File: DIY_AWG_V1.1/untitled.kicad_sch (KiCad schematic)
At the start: 61 parts, among them U1 AMS1117-3.3, U2 ADP7118ARDZ-3.3-R7, U3 ADP7118ARDZ-3.3-R7, U4 TPS7A3301RGWR, U5 TPS7A4701RGWR, U6 TPS7A3301RGWR, U7 TPS7A4701RGWR

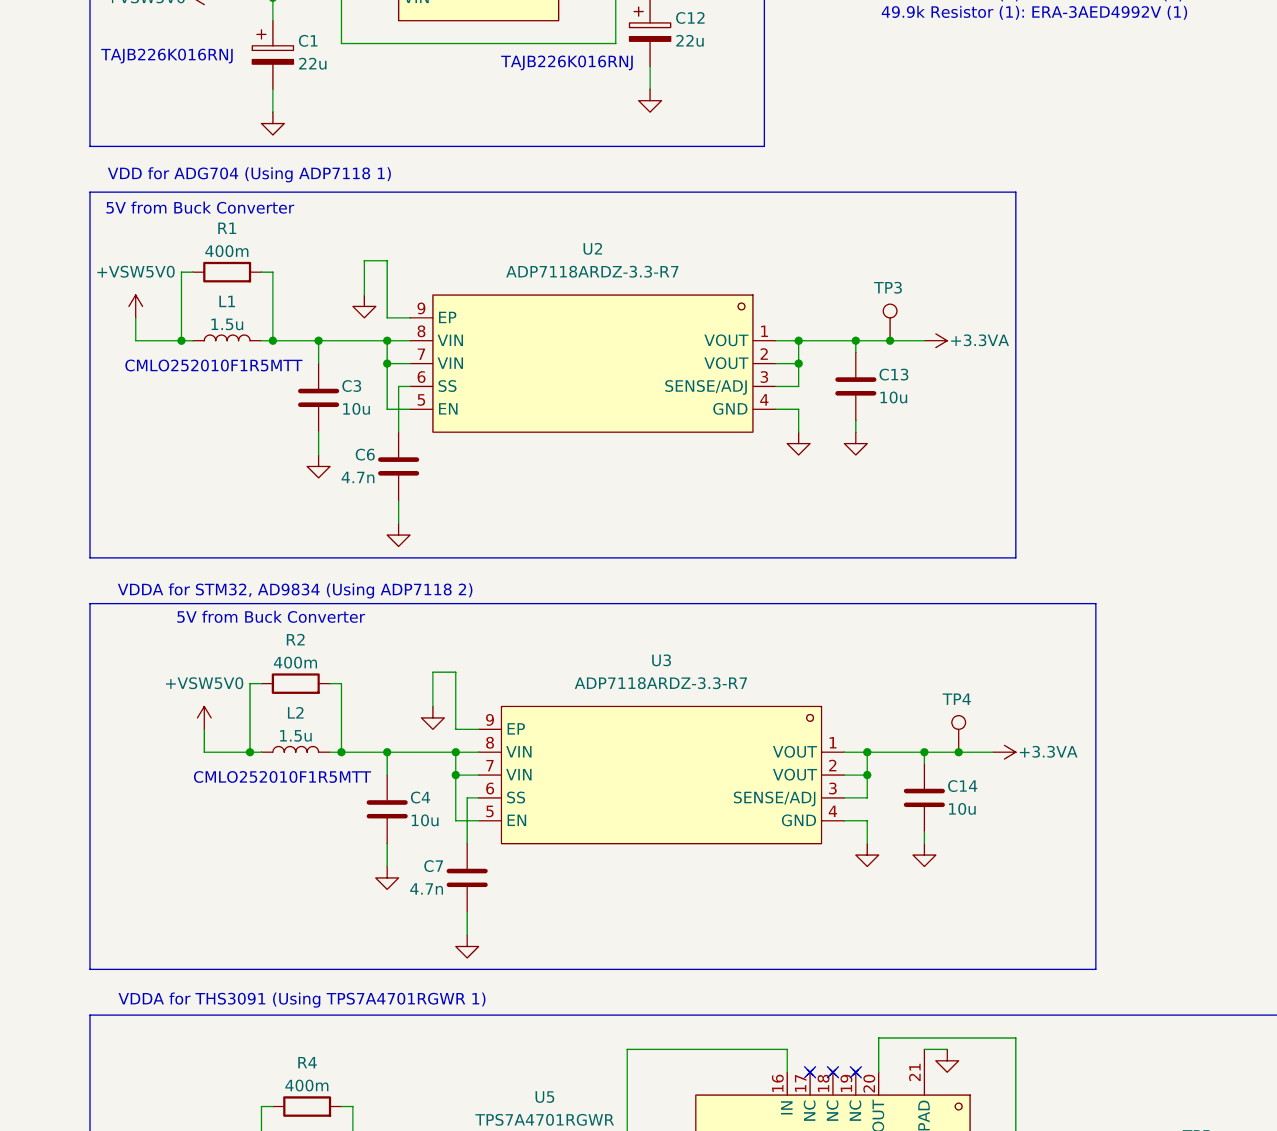
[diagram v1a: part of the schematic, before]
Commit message: Updated pin description of relevant components
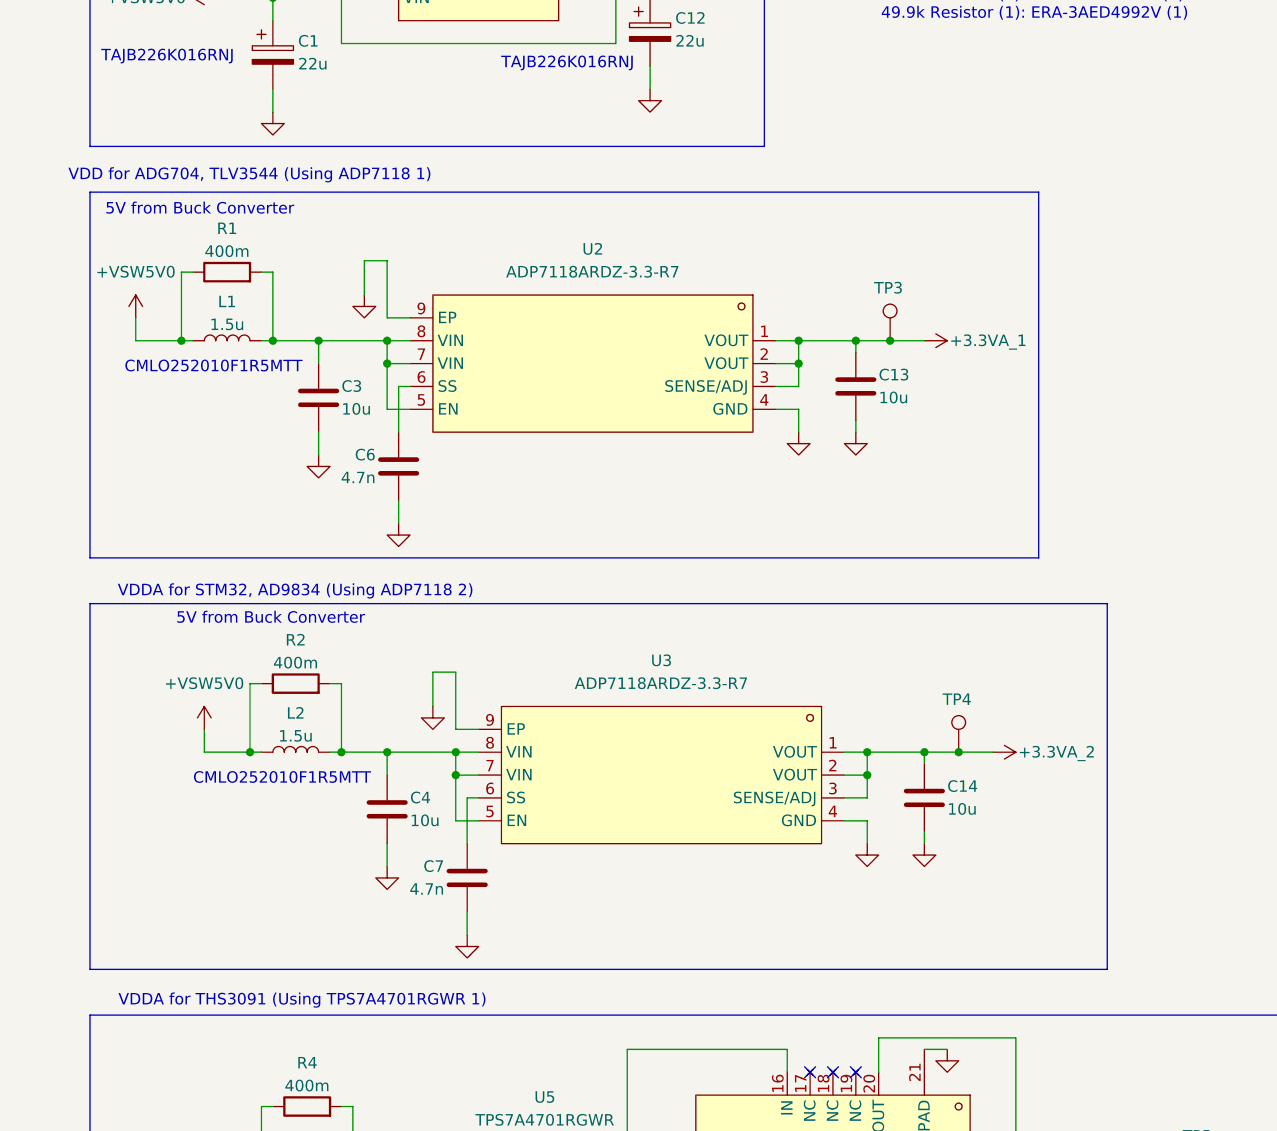
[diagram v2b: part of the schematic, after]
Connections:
- net +3.3VA renamed +3.3VA_1
- net +3.3VA_1: no longer C14.1, TP4.1, U3.1 (VOUT), U3.2 (VOUT), U3.3 (SENSE/ADJ)
- new net +3.3VA_2: C14.1, TP4.1, U3.1 (VOUT), U3.2 (VOUT), U3.3 (SENSE/ADJ)
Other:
- note added: "VDD for ADG704, TLV3544 (Using ADP7118 1)"
- note removed: "VDD for ADG704 (Using ADP7118 1)"
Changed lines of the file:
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@@
 	(rectangle
 		(start 15.24 118.11)
-		(end 127 158.75)
+		(end 128.27 158.75)
 		(stroke
 			(width 0)
@@
 	(rectangle
 		(start 15.24 72.39)
-		(end 118.11 113.03)
+		(end 120.65 113.03)
 		(stroke
 			(width 0)
@@
 		)
 	)
-	(text "VDD for ADG704 (Using ADP7118 1)\n\n"
+	(text "VDD for ADG704, TLV3544 (Using ADP7118 1)\n\n"
 		(exclude_from_sim no)
 		(at 33.02 71.628 0)
@@
 			)
 		)
-		(property "Value" "+3.3VA"
+		(property "Value" "+3.3VA_1"
 			(at 110.744 88.9 90)
 			(show_name no)
@@
 			)
 		)
-		(property "Value" "+3.3VA"
+		(property "Value" "+3.3VA_2"
 			(at 118.364 134.62 90)
 			(show_name no)

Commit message: Updated schematics to clear ERCs
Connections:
- net at C20.1, C22.1, L5.2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: now also U6.13 (EN)

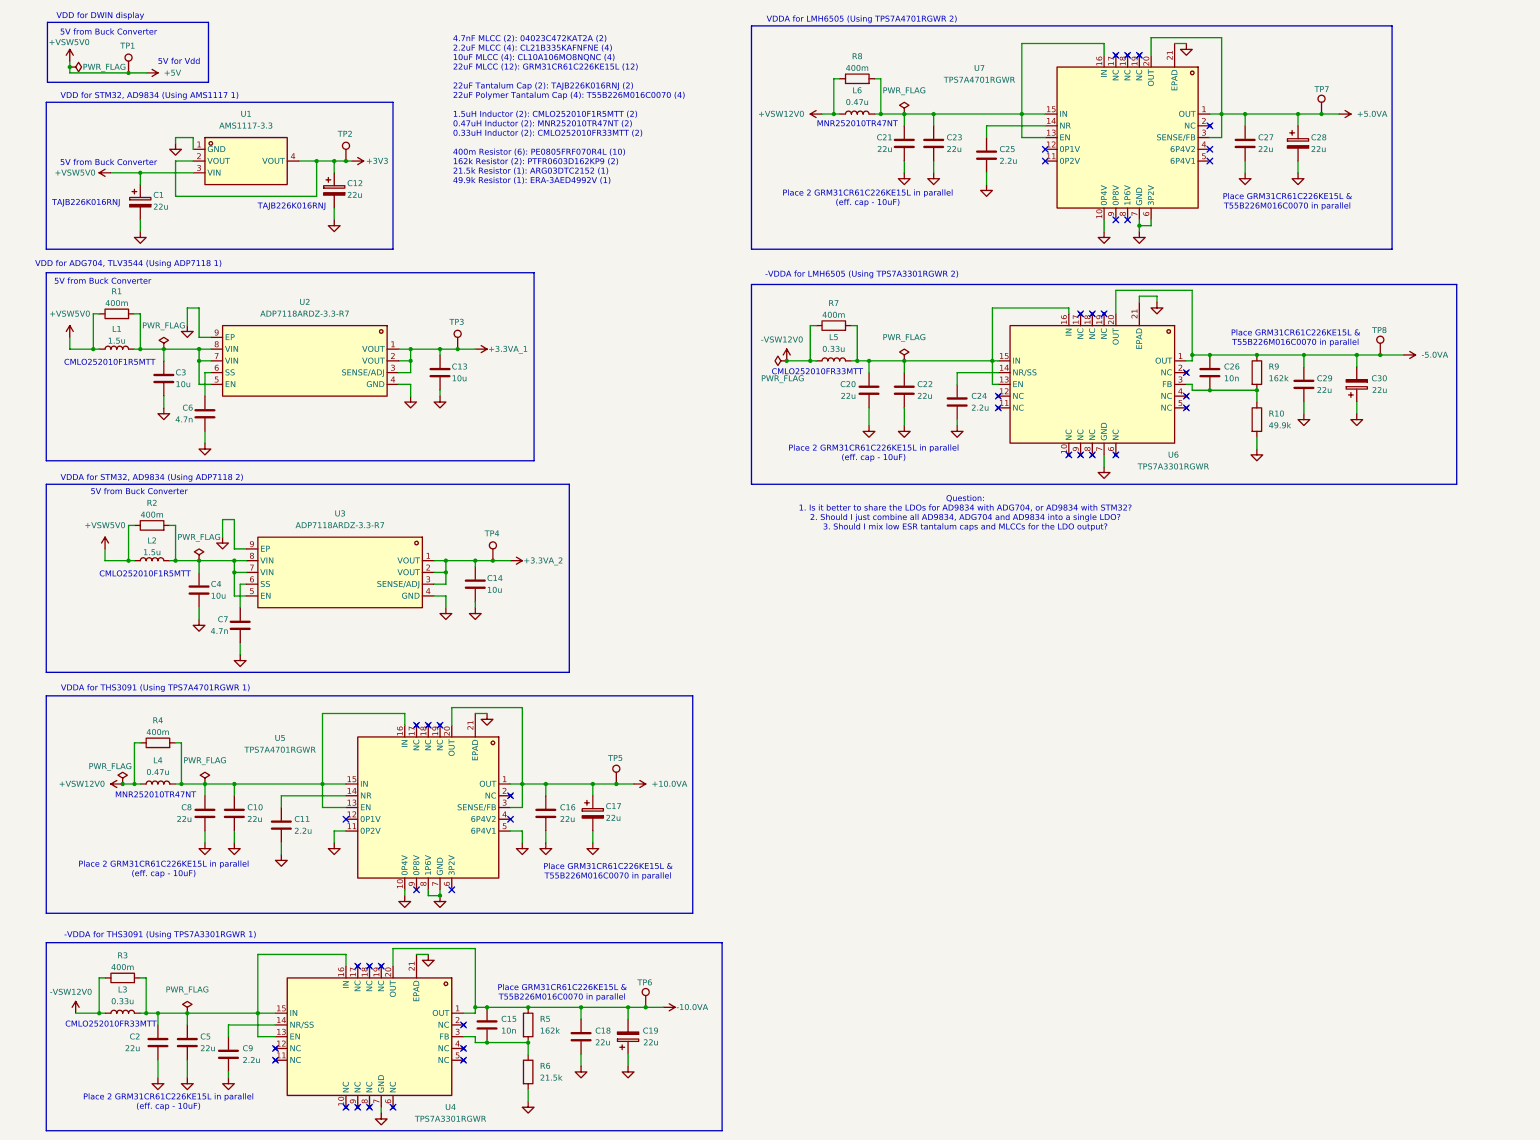
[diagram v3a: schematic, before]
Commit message: Updated to fix all ERCs
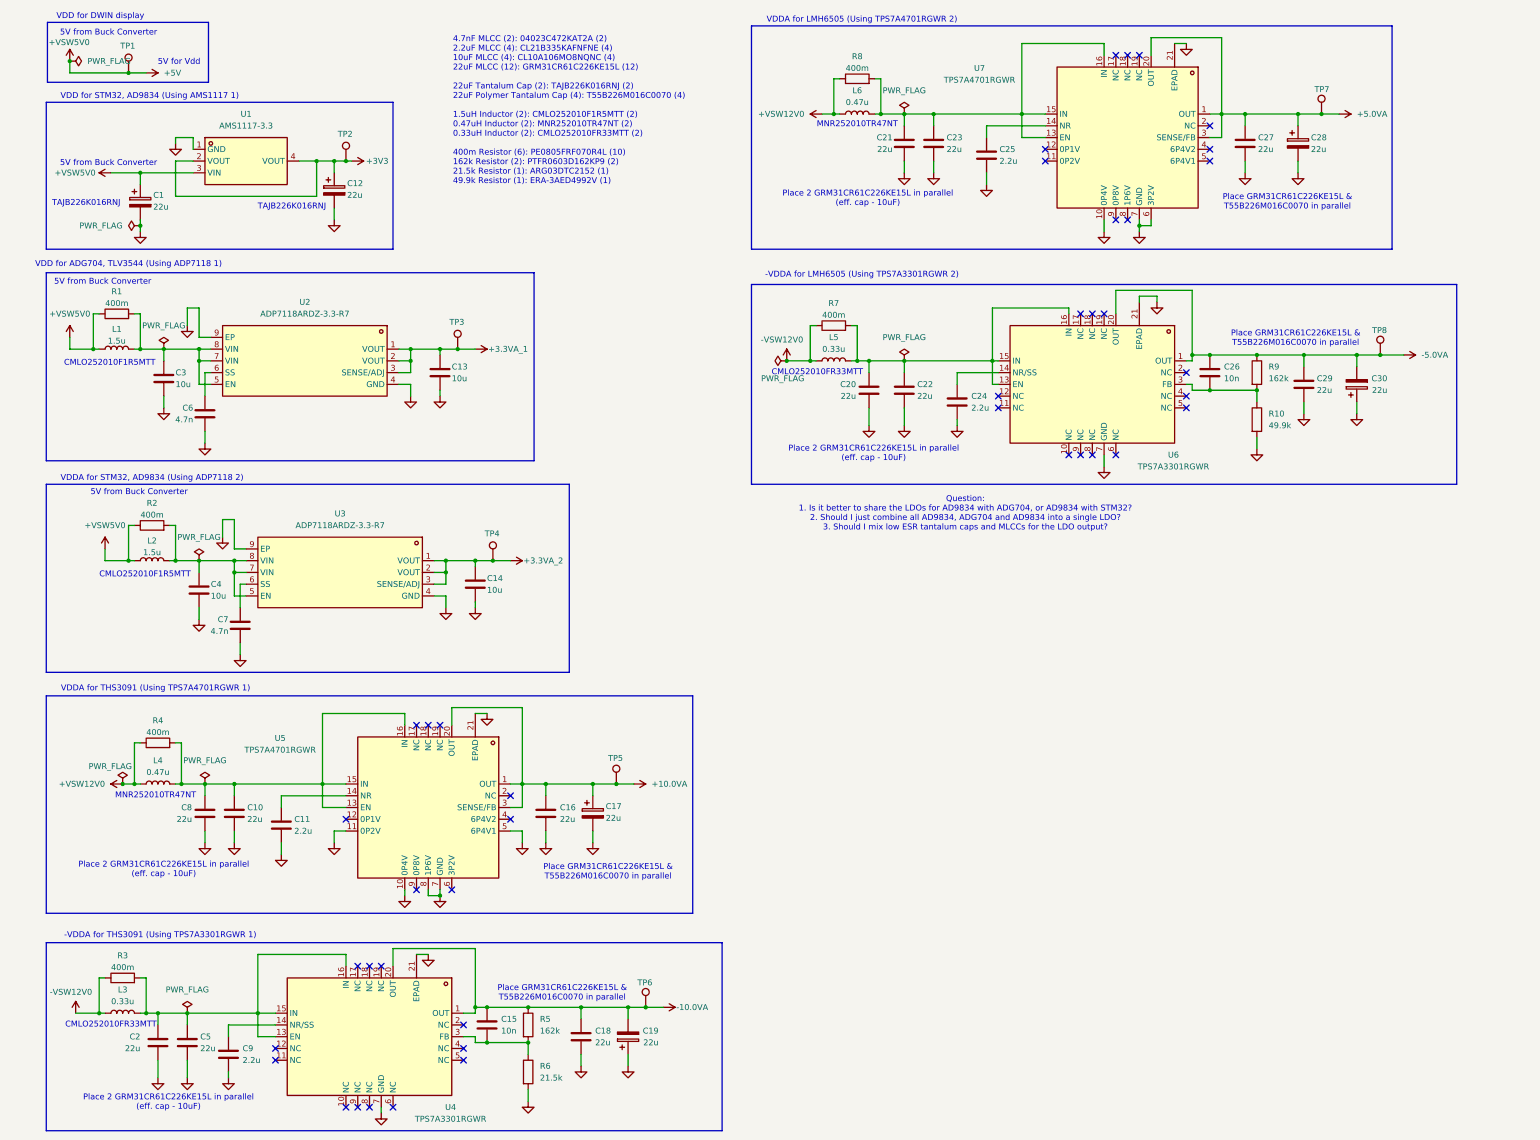
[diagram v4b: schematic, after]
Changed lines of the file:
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@@
 	)
 	(junction
-		(at 20.32 27.94)
-		(diameter 0)
-		(color 0 0 0 0)
-	)
-	(junction
 		(at 219.71 91.44)
 		(diameter 0)
@@
 	)
 	(junction
+		(at 20.32 26.67)
+		(diameter 0)
+		(color 0 0 0 0)
+	)
+	(junction
 		(at 44.45 182.88)
 		(diameter 0)
@@
 	)
 	(junction
+		(at 35.56 62.23)
+		(diameter 0)
+		(color 0 0 0 0)
+	)
+	(junction
 		(at 101.6 134.62)
 		(diameter 0)
@@
 	(wire
 		(pts
-			(xy 20.32 26.67) (xy 20.32 27.94)
+			(xy 20.32 26.67) (xy 20.32 29.21)
 		)
 		(stroke
@@
 	(wire
 		(pts
-			(xy 20.32 27.94) (xy 20.32 29.21)
-		)
-		(stroke
-			(width 0)
-			(type default)
-		)
-	)
-	(wire
-		(pts
 			(xy 97.79 207.01) (xy 100.33 207.01)
 		)
@@
 	(wire
 		(pts
+			(xy 35.56 62.23) (xy 35.56 63.5)
+		)
+		(stroke
+			(width 0)
+			(type default)
+		)
+	)
+	(wire
+		(pts
 			(xy 200.66 48.26) (xy 200.66 50.8)
 		)
@@
 	(wire
 		(pts
-			(xy 35.56 60.96) (xy 35.56 63.5)
+			(xy 35.56 60.96) (xy 35.56 62.23)
 		)
 		(stroke
@@
 	)
 	(symbol
+		(lib_id "power:PWR_FLAG")
+		(at 20.32 26.67 270)
+		(unit 1)
+		(body_style 1)
+		(exclude_from_sim no)
+		(in_bom yes)
+		(on_board yes)
+		(in_pos_files yes)
+		(dnp no)
+		(fields_autoplaced yes)
+		(property "Reference" "#FLG017"
+			(at 22.225 26.67 0)
+			(hide yes)
+			(show_name no)
+			(do_not_autoplace no)
+			(effects
+				(font
+					(size 1.27 1.27)
+				)
+			)
+		)
+		(property "Value" "PWR_FLAG"
+			(at 24.13 26.6699 90)
+			(show_name no)
+			(do_not_autoplace no)
+			(effects
+				(font
+					(size 1.27 1.27)
+				)
+				(justify left)
+			)
+		)
+		(property "Footprint" ""
+			(at 20.32 26.67 0)
+			(hide yes)
+			(show_name no)
+			(do_not_autoplace no)
+			(effects
+				(font
+					(size 1.27 1.27)
+				)
+			)
+		)
+		(property "Datasheet" ""
+			(at 20.32 26.67 0)
+			(hide yes)
+			(show_name no)
+			(do_not_autoplace no)
+			(effects
+				(font
+					(size 1.27 1.27)
+				)
+			)
+		)
+		(property "Description" "Special symbol for telling ERC where power comes from"
+			(at 20.32 26.67 0)
+			(hide yes)
+			(show_name no)
+			(do_not_autoplace no)
+			(effects
+				(font
+					(size 1.27 1.27)
+				)
+			)
+		)
+		(pin "1"
+		)
+		(instances
+			(project "DIY_AWG_V1.1"
+				(path "/508078af-d961-4af3-840e-a064a9f8d5bc/8acbd35e-0359-4140-a5a5-b9cabf9b139d"
+					(reference "#FLG017")
+					(unit 1)
+				)
+			)
+		)
+	)
+	(symbol
 		(lib_id "Device:C")
 		(at 66.04 191.77 0)
@@
 	)
 	(symbol
-		(lib_name "TPS7A4701RGWR_1")
 		(lib_id "easyeda2kicad:TPS7A4701RGWR")
 		(at 248.92 41.91 0)
@@
 	)
 	(symbol
-		(lib_name "AMS1117-3.3_1")
 		(lib_id "easyeda2kicad:AMS1117-3.3")
 		(at 58.42 48.26 0)
@@
 	)
 	(symbol
-		(lib_name "TPS7A3301RGWR_1")
 		(lib_id "easyeda2kicad:TPS7A3301RGWR")
 		(at 241.3 95.25 0)
@@
 	)
 	(symbol
+		(lib_id "power:PWR_FLAG")
+		(at 35.56 62.23 90)
+		(unit 1)
+		(body_style 1)
+		(exclude_from_sim no)
+		(in_bom yes)
+		(on_board yes)
+		(in_pos_files yes)
+		(dnp no)
+		(fields_autoplaced yes)
+		(property "Reference" "#FLG018"
+			(at 33.655 62.23 0)
+			(hide yes)
+			(show_name no)
+			(do_not_autoplace no)
+			(effects
+				(font
+					(size 1.27 1.27)
+				)
+			)
+		)
+		(property "Value" "PWR_FLAG"
+			(at 31.75 62.2299 90)
+			(show_name no)
+			(do_not_autoplace no)
+			(effects
+				(font
+					(size 1.27 1.27)
+				)
+				(justify left)
+			)
+		)
+		(property "Footprint" ""
+			(at 35.56 62.23 0)
+			(hide yes)
+			(show_name no)
+			(do_not_autoplace no)
+			(effects
+				(font
+					(size 1.27 1.27)
+				)
+			)
+		)
+		(property "Datasheet" ""
+			(at 35.56 62.23 0)
+			(hide yes)
+			(show_name no)
+			(do_not_autoplace no)
+			(effects
+				(font
+					(size 1.27 1.27)
+				)
+			)
+		)
+		(property "Description" "Special symbol for telling ERC where power comes from"
+			(at 35.56 62.23 0)
+			(hide yes)
+			(show_name no)
+			(do_not_autoplace no)
+			(effects
+				(font
+					(size 1.27 1.27)
+				)
+			)
+		)
+		(pin "1"
+		)
+		(instances
+			(project "DIY_AWG_V1.1"
+				(path "/508078af-d961-4af3-840e-a064a9f8d5bc/8acbd35e-0359-4140-a5a5-b9cabf9b139d"
+					(reference "#FLG018")
+					(unit 1)
+				)
+			)
+		)
+	)
+	(symbol
 		(lib_id "Device:R")
 		(at 185.42 83.82 90)
@@
 	)
 	(symbol
-		(lib_name "ADP7118ARDZ-3.3-R7_1")
 		(lib_id "easyeda2kicad:ADP7118ARDZ-3.3-R7")
 		(at 71.12 91.44 0)
@@
 	)
 	(symbol
-		(lib_name "TPS7A4701RGWR_1")
 		(lib_id "easyeda2kicad:TPS7A4701RGWR")
 		(at 97.79 186.69 0)
@@
 	)
 	(symbol
-		(lib_name "TPS7A3301RGWR_1")
 		(lib_id "easyeda2kicad:TPS7A3301RGWR")
 		(at 85.09 236.22 0)
@@
 					(unit 1)
 				)
-			)
-		)
-	)
-	(symbol
-		(lib_id "power:PWR_FLAG")
-		(at 20.32 27.94 270)
-		(unit 1)
-		(body_style 1)
-		(exclude_from_sim no)
-		(in_bom yes)
-		(on_board yes)
-		(in_pos_files yes)
-		(dnp no)
-		(property "Reference" "#FLG04"
-			(at 22.225 27.94 0)
-			(hide yes)
-			(show_name no)
-			(do_not_autoplace no)
-			(effects
-				(font
-					(size 1.27 1.27)
-				)
-			)
-		)
-		(property "Value" "PWR_FLAG"
-			(at 23.114 27.94 90)
-			(show_name no)
-			(do_not_autoplace no)
-			(effects
-				(font
-					(size 1.27 1.27)
-				)
-				(justify left)
-			)
-		)
-		(property "Footprint" ""
-			(at 20.32 27.94 0)
-			(hide yes)
-			(show_name no)
-			(do_not_autoplace no)
-			(effects
-				(font
-					(size 1.27 1.27)
-				)
-			)
-		)
-		(property "Datasheet" ""
-			(at 20.32 27.94 0)
-			(hide yes)
-			(show_name no)
-			(do_not_autoplace no)
-			(effects
-				(font
-					(size 1.27 1.27)
-				)
-			)
-		)
-		(property "Description" "Special symbol for telling ERC where power comes from"
-			(at 20.32 27.94 0)
-			(hide yes)
-			(show_name no)
-			(do_not_autoplace no)
-			(effects
-				(font
-					(size 1.27 1.27)
-				)
-			)
-		)
-		(pin "1"
-		)
-		(instances
-			(project "DIY_AWG_V1.1"
-				(path "/508078af-d961-4af3-840e-a064a9f8d5bc/8acbd35e-0359-4140-a5a5-b9cabf9b139d"
-					(reference "#FLG04")
-					(unit 1)
-				)
